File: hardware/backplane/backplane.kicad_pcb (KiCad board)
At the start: 2 copper layers, 200 x 124 mm, 104 parts, among them J1 C96ABC, J10 Conn_Coaxial_Power, J2 C96ABC, J3 C96ABC, J4 C96ABC, J5 C96ABC, J6 C96ABC, J7 C96ABC, J8 C96ABC, J9 C96ABC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

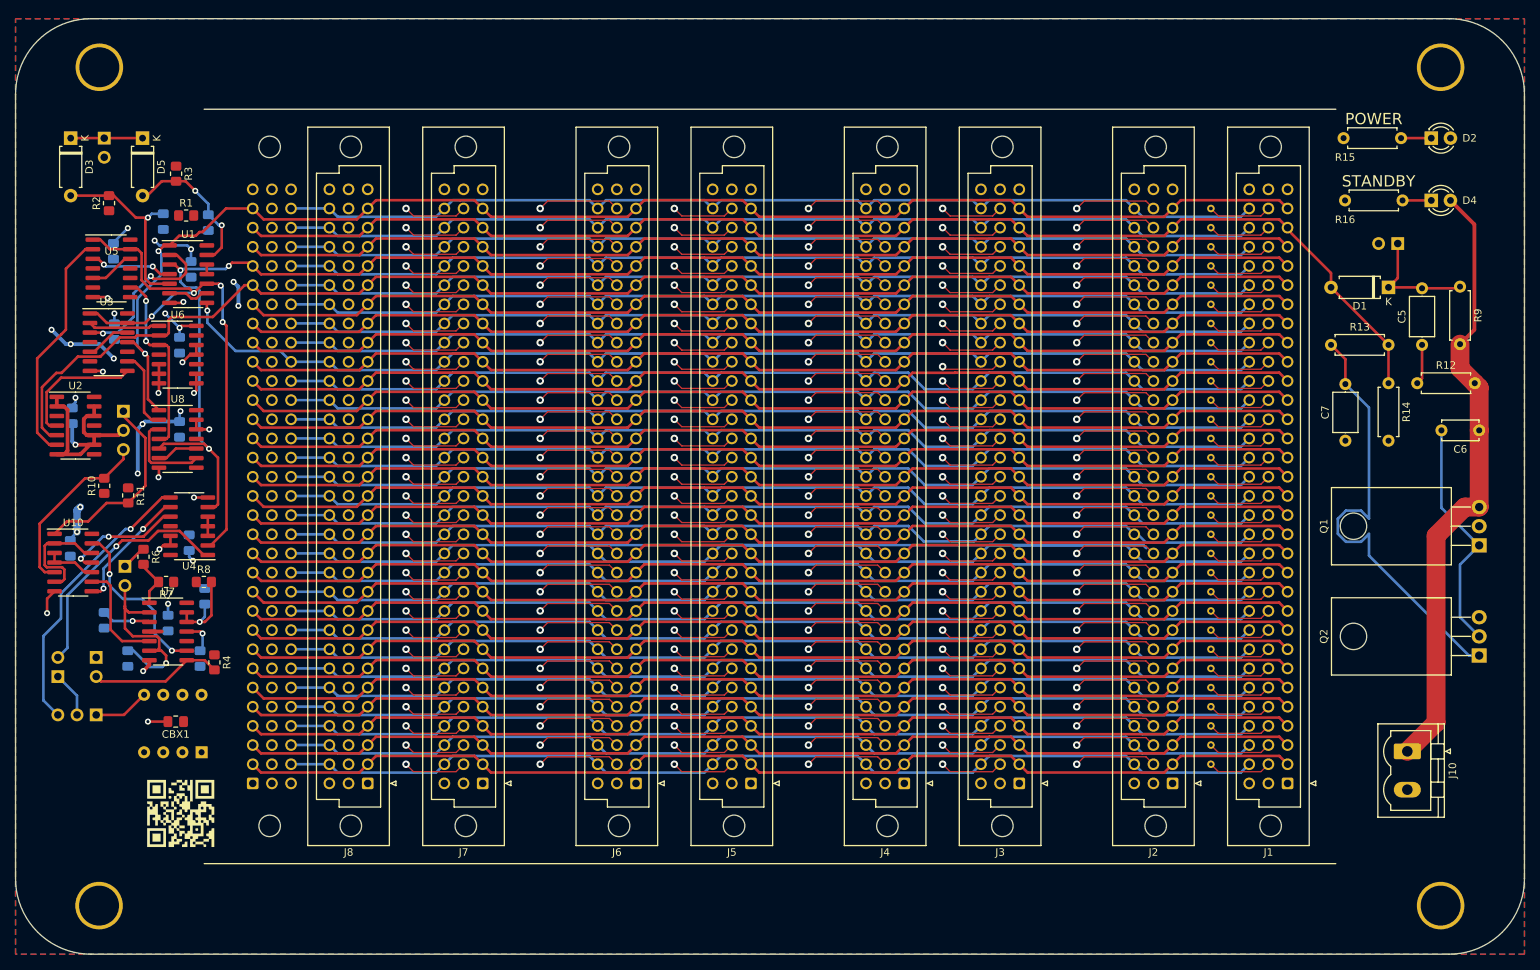
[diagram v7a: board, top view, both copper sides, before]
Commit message: backplane: minor improvements
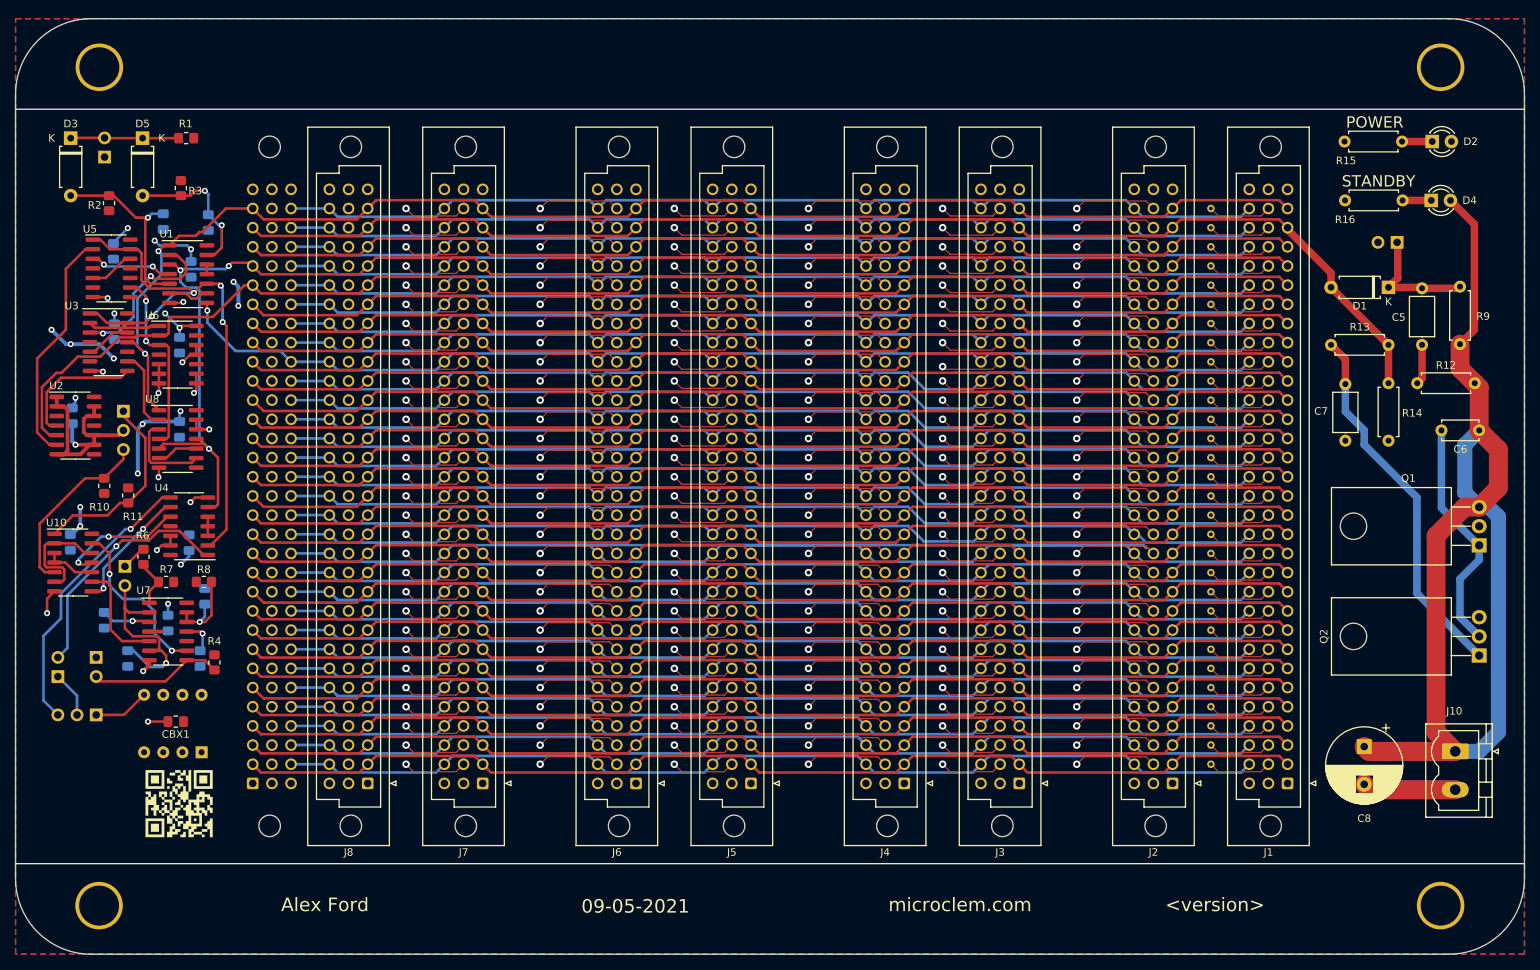
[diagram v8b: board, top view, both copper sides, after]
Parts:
- removed JPC1: JP_RST, Connector_PinHeader_2.54mm:PinHeader_1x02_P2.54mm_Vertical
- removed JPC2: JP_PWR_BTN, Connector_PinHeader_2.54mm:PinHeader_1x02_P2.54mm_Vertical
- added C8: CP, Capacitor_THT:CP_Radial_D10.0mm_P5.00mm, F.Cu at (222.8, 125.0)
- added SW4: SW_Push, Connector_PinHeader_2.54mm:PinHeader_1x02_P2.54mm_Vertical, B.Cu at (55.9, 46.9)
- added SW5: SW_Push, Connector_PinHeader_2.54mm:PinHeader_1x02_P2.54mm_Vertical, B.Cu at (227.2, 58.2)
- moved R1 10.3 mm to (66.7, 44.4), turned to 180 degrees
- moved J10 6.35 mm to (234.9, 125.6)
- moved R3 2.01 mm to (66.0, 51.0)
- moved G*** 1.32 mm to (65.8, 132.6)
- moved CBU10 0.80 mm to (51.3, 97.9)
- moved G*** 0.67 mm to (53.3, 131.3)
- moved D2 0.47 mm to (231.9, 44.8)
- moved R15 0.47 mm to (220.2, 44.8)
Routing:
- net +5V: track 81.2 -> 170.1 mm
- net GND: track 64.9 -> 90.7 mm
- net Net-(C7-Pad2): track 60.1 -> 49.3 mm
- net ~RST_HDR~: track 9.52 -> 14.4 mm
- net Net-(U10-Pad11): track 15.9 -> 17.0 mm
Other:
- board text added: "09-05-2021"
- board text added: "555_ADJ"
- board text added: "555_STEP"
- board text added: "<version>"
- board text added: "AST_MONO_SW"
- board text added: "Alex Ford"
- board text added: "CLK_EN"
- board text added: "CLK_SEL"
- board text added: "POWER_SW"
- board text added: "RESET_SW"
- board text added: "microclem.com"
- board text removed: "RESET"
